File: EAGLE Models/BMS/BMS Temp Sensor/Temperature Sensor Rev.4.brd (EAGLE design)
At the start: 16 x 22 mm, 7 parts

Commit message: Set Resistance Values for the Temp Sense Board and Fixed ADC Connections
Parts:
- R2: value (none) -> 10k
- T$1: value THERMISTOR -> 10k
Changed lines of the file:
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@@
 <element name="G_OUT" library="wirepad" package="1,6/0,8" value="" x="2.54" y="3.81"/>
 <element name="OUTPUT" library="wirepad" package="1,6/0,8" value="" x="12.7" y="3.81"/>
-<element name="R2" library="resistor" package="R0603" value="" x="4.445" y="11.43" rot="R90"/>
-<element name="T$1" library="formula electric" package="0603" value="THERMISTOR" x="9.525" y="11.43" rot="R270"/>
+<element name="R2" library="resistor" package="R0603" value="10k" x="4.445" y="11.43" rot="R90"/>
+<element name="T$1" library="formula electric" package="0603" value="10k" x="9.525" y="11.43" rot="R270"/>
 <element name="VCC_IN" library="wirepad" package="1,6/0,8" value="" x="7.62" y="15.875"/>
 <element name="VCC_OUT" library="wirepad" package="1,6/0,8" value="" x="7.62" y="3.81"/>

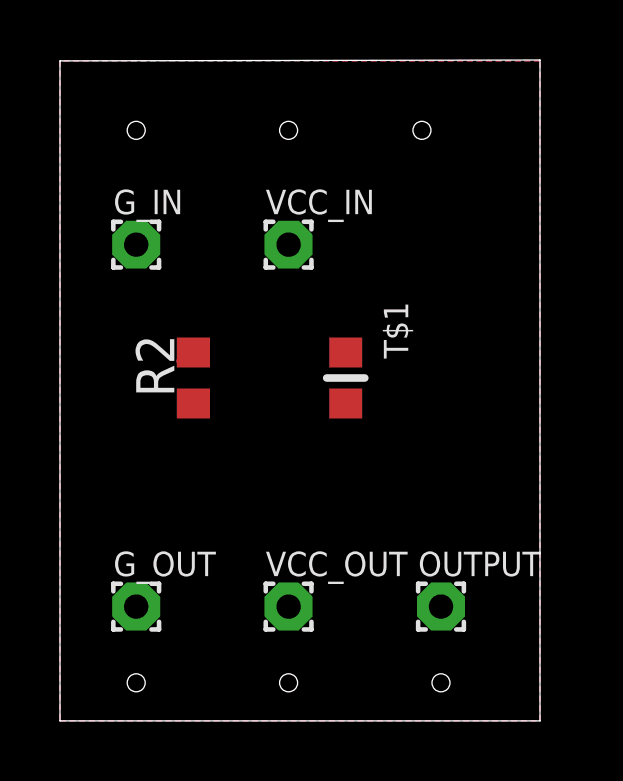
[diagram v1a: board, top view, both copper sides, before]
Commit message: Temp Sense Board Layouts Finished First revision, bunch of test layouts to get estimate of board sizes
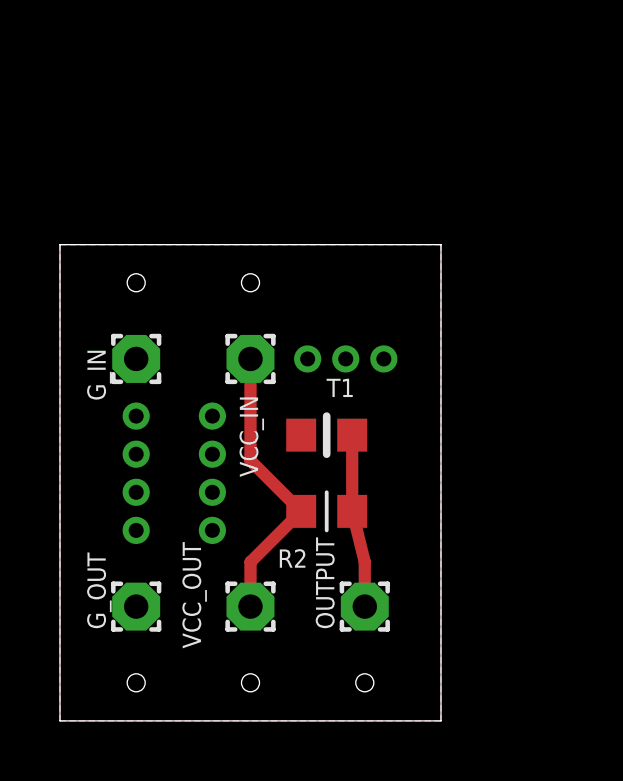
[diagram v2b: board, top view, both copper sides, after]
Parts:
- removed T$1: 10k, formula electric:0603
- added T1: 10k, formula electric:0603
- moved R2 6.29 mm to (8.89, 6.99), turned to 0 degrees
- moved VCC_IN 4.02 mm to (6.35, 12.1), turned to 90 degrees
- moved G_IN 3.81 mm to (2.54, 12.1), turned to 90 degrees
- moved OUTPUT 2.54 mm to (10.2, 3.81), turned to 90 degrees
- moved VCC_OUT 1.27 mm to (6.35, 3.81), turned to 90 degrees
- turned G_OUT to 90 degrees
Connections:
- net GND: now also T1.P$2; no longer T$1.P$2
- net OUTPUT: now also T1.P$1; no longer T$1.P$1
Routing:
- net VCC: track 0.00 -> 9.66 mm
- net OUTPUT: track 0.53 -> 5.77 mm
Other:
- board size 16 x 22 mm -> 12.7 x 15.9 mm
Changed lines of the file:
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@@
 <setting verticaltext="up"/>
 </settings>
-<grid distance="0.05" unitdist="inch" unit="mm" style="lines" multiple="1" display="no" altdistance="0.025" altunitdist="inch" altunit="inch"/>
+<grid distance="0.05" unitdist="inch" unit="inch" style="lines" multiple="1" display="no" altdistance="0.025" altunitdist="inch" altunit="inch"/>
 <layers>
 <layer number="1" name="Top" color="4" fill="1" visible="yes" active="yes"/>
@@
 <board>
 <plain>
-<wire x1="0" y1="0" x2="16" y2="0" width="0" layer="20"/>
-<wire x1="16" y1="0" x2="16" y2="22.03" width="0" layer="20"/>
-<wire x1="16" y1="22.03" x2="0" y2="22" width="0" layer="20"/>
-<wire x1="0" y1="22" x2="0" y2="0" width="0" layer="20"/>
+<wire x1="0" y1="0" x2="12.7" y2="0" width="0" layer="20"/>
+<wire x1="12.7" y1="0" x2="12.7" y2="15.875" width="0" layer="20"/>
+<wire x1="12.7" y1="15.875" x2="0" y2="15.875" width="0" layer="20"/>
+<wire x1="0" y1="15.875" x2="0" y2="0" width="0" layer="20"/>
 <hole x="2.54" y="1.27" drill="0.6"/>
-<hole x="7.62" y="1.27" drill="0.6"/>
-<hole x="12.7" y="1.27" drill="0.6"/>
-<hole x="12.065" y="19.685" drill="0.6"/>
-<hole x="7.62" y="19.685" drill="0.6"/>
-<hole x="2.54" y="19.685" drill="0.6"/>
+<hole x="6.35" y="1.27" drill="0.6"/>
+<hole x="10.16" y="1.27" drill="0.6"/>
+<hole x="6.35" y="14.605" drill="0.6"/>
+<hole x="2.54" y="14.605" drill="0.6"/>
 </plain>
 <attributes>
@@
 </class>
 </classes>
-<designrules name="default">
+<designrules name="default *">
 <description language="de">&lt;b&gt;EAGLE Design Rules&lt;/b&gt;
 &lt;p&gt;
@@
 <param name="mtCopper" value="0.035mm 0.035mm 0.035mm 0.035mm 0.035mm 0.035mm 0.035mm 0.035mm 0.035mm 0.035mm 0.035mm 0.035mm 0.035mm 0.035mm 0.035mm 0.035mm"/>
 <param name="mtIsolate" value="1.5mm 0.15mm 0.2mm 0.15mm 0.2mm 0.15mm 0.2mm 0.15mm 0.2mm 0.15mm 0.2mm 0.15mm 0.2mm 0.15mm 0.2mm"/>
-<param name="mdWireWire" value="8mil"/>
-<param name="mdWirePad" value="8mil"/>
-<param name="mdWireVia" value="8mil"/>
-<param name="mdPadPad" value="8mil"/>
-<param name="mdPadVia" value="8mil"/>
-<param name="mdViaVia" value="8mil"/>
-<param name="mdSmdPad" value="8mil"/>
-<param name="mdSmdVia" value="8mil"/>
-<param name="mdSmdSmd" value="8mil"/>
+<param name="mdWireWire" value="6mil"/>
+<param name="mdWirePad" value="6mil"/>
+<param name="mdWireVia" value="6mil"/>
+<param name="mdPadPad" value="6mil"/>
+<param name="mdPadVia" value="6mil"/>
+<param name="mdViaVia" value="6mil"/>
+<param name="mdSmdPad" value="6mil"/>
+<param name="mdSmdVia" value="6mil"/>
+<param name="mdSmdSmd" value="6mil"/>
 <param name="mdViaViaSameLayer" value="8mil"/>
 <param name="mnLayersViaInSmd" value="2"/>
@@
 <param name="mdDrill" value="8mil"/>
 <param name="mdSmdStop" value="0mil"/>
-<param name="msWidth" value="10mil"/>
-<param name="msDrill" value="24mil"/>
+<param name="msWidth" value="6mil"/>
+<param name="msDrill" value="13mil"/>
 <param name="msMicroVia" value="9.99mm"/>
 <param name="msBlindViaRatio" value="0.5"/>
@@
 <param name="srMinRoundness" value="0mil"/>
 <param name="srMaxRoundness" value="0mil"/>
-<param name="slThermalIsolate" value="10mil"/>
+<param name="slThermalIsolate" value="6mil"/>
 <param name="slThermalsForVias" value="0"/>
 <param name="dpMaxLengthDifference" value="10mm"/>
@@
 </autorouter>
 <elements>
-<element name="G_IN" library="wirepad" package="1,6/0,8" value="" x="2.54" y="15.875"/>
-<element name="G_OUT" library="wirepad" package="1,6/0,8" value="" x="2.54" y="3.81"/>
-<element name="OUTPUT" library="wirepad" package="1,6/0,8" value="" x="12.7" y="3.81"/>
-<element name="R2" library="resistor" package="R0603" value="10k" x="4.445" y="11.43" rot="R90"/>
-<element name="T$1" library="formula electric" package="0603" value="10k" x="9.525" y="11.43" rot="R270"/>
-<element name="VCC_IN" library="wirepad" package="1,6/0,8" value="" x="7.62" y="15.875"/>
-<element name="VCC_OUT" library="wirepad" package="1,6/0,8" value="" x="7.62" y="3.81"/>
+<element name="G_IN" library="wirepad" package="1,6/0,8" value="" x="2.54" y="12.065" smashed="yes" rot="R90">
+<attribute name="NAME" x="1.524" y="10.668" size="0.6096" layer="25" ratio="10" rot="R90"/>
+<attribute name="VALUE" x="1.94" y="12.065" size="0.0254" layer="27" rot="R90"/>
+</element>
+<element name="G_OUT" library="wirepad" package="1,6/0,8" value="" x="2.54" y="3.81" smashed="yes" rot="R90">
+<attribute name="NAME" x="1.524" y="3.048" size="0.6096" layer="25" ratio="10" rot="R90"/>
+<attribute name="VALUE" x="1.94" y="3.81" size="0.0254" layer="27" rot="R90"/>
+</element>
+<element name="OUTPUT" library="wirepad" package="1,6/0,8" value="" x="10.16" y="3.81" smashed="yes" rot="R90">
+<attribute name="NAME" x="9.144" y="3.048" size="0.6096" layer="25" ratio="10" rot="R90"/>
+<attribute name="VALUE" x="9.56" y="3.81" size="0.0254" layer="27" rot="R90"/>
+</element>
+<element name="R2" library="resistor" package="R0603" value="10k" x="8.89" y="6.985" smashed="yes">
+<attribute name="NAME" x="8.255" y="5.715" size="0.6096" layer="25" rot="R180"/>
+<attribute name="VALUE" x="10.795" y="7.62" size="0.6096" layer="27" rot="R270"/>
+</element>
+<element name="T1" library="formula electric" package="0603" value="10k" x="8.89" y="9.525" smashed="yes" rot="R180">
+<attribute name="NAME" x="8.89" y="10.795" size="0.6096" layer="25"/>
+<attribute name="VALUE" x="10.795" y="10.16" size="0.6096" layer="27" rot="R270"/>
+</element>
+<element name="VCC_IN" library="wirepad" package="1,6/0,8" value="" x="6.35" y="12.065" smashed="yes" rot="R90">
+<attribute name="NAME" x="6.604" y="8.128" size="0.6096" layer="25" ratio="10" rot="R90"/>
+<attribute name="VALUE" x="5.75" y="12.065" size="0.0254" layer="27" rot="R90"/>
+</element>
+<element name="VCC_OUT" library="wirepad" package="1,6/0,8" value="" x="6.35" y="3.81" smashed="yes" rot="R90">
+<attribute name="NAME" x="4.699" y="2.413" size="0.6096" layer="25" ratio="10" rot="R90"/>
+<attribute name="VALUE" x="5.75" y="3.81" size="0.0254" layer="27" rot="R90"/>
+</element>
 </elements>
 <signals>
@@
 <contactref element="VCC_IN" pad="1"/>
 <contactref element="VCC_OUT" pad="1"/>
-<wire x1="4.445" y1="10.58" x2="7.62" y2="15.875" width="0" layer="19" extent="16-16"/>
-<wire x1="7.62" y1="3.81" x2="4.445" y2="10.58" width="0" layer="19" extent="16-16"/>
+<wire x1="6.35" y1="3.81" x2="6.35" y2="5.295" width="0.4064" layer="1"/>
+<wire x1="6.35" y1="5.295" x2="8.04" y2="6.985" width="0.4064" layer="1"/>
+<wire x1="8.04" y1="6.985" x2="6.35" y2="8.675" width="0.4064" layer="1"/>
+<wire x1="6.35" y1="8.675" x2="6.35" y2="12.065" width="0.4064" layer="1"/>
 </signal>
 <signal name="GND">
-<contactref element="T$1" pad="P$2"/>
+<contactref element="T1" pad="P$2"/>
 <contactref element="G_IN" pad="1"/>
 <contactref element="G_OUT" pad="1"/>
 <polygon width="0.4064" layer="1" isolate="0.3048">
 <vertex x="0" y="0"/>
-<vertex x="16" y="0"/>
-<vertex x="16" y="22"/>
-<vertex x="0" y="22"/>
+<vertex x="12.7" y="0"/>
+<vertex x="12.7" y="15.875"/>
+<vertex x="0" y="15.875"/>
 </polygon>
 <polygon width="0.4064" layer="16" isolate="0.3048">
 <vertex x="0" y="0"/>
-<vertex x="16" y="0"/>
-<vertex x="16" y="22"/>
-<vertex x="0" y="22"/>
+<vertex x="12.7" y="0"/>
+<vertex x="12.7" y="15.875"/>
+<vertex x="0" y="15.875"/>
 </polygon>
-<wire x1="9.525" y1="10.58" x2="2.54" y2="15.875" width="0" layer="19" extent="1-1"/>
-<wire x1="2.54" y1="3.81" x2="9.525" y2="10.58" width="0" layer="19" extent="1-1"/>
+<via x="2.54" y="10.16" extent="1-16" drill="0.5"/>
+<via x="2.54" y="8.89" extent="1-16" drill="0.5"/>
+<via x="2.54" y="7.62" extent="1-16" drill="0.5"/>
+<via x="2.54" y="6.35" extent="1-16" drill="0.5"/>
+<via x="5.08" y="6.35" extent="1-16" drill="0.5"/>
+<via x="5.08" y="7.62" extent="1-16" drill="0.5"/>
+<via x="5.08" y="8.89" extent="1-16" drill="0.5"/>
+<via x="5.08" y="10.16" extent="1-16" drill="0.5"/>
+<via x="8.255" y="12.065" extent="1-16" drill="0.5"/>
+<via x="9.525" y="12.065" extent="1-16" drill="0.5"/>
+<via x="10.795" y="12.065" extent="1-16" drill="0.5"/>
 </signal>
 <signal name="OUTPUT">
 <contactref element="OUTPUT" pad="1"/>
-<contactref element="T$1" pad="P$1"/>
+<contactref element="T1" pad="P$1"/>
 <contactref element="R2" pad="2"/>
-<wire x1="4" y1="12" x2="4.445" y2="12.28" width="0.254" layer="1"/>
-<wire x1="9.525" y1="12.28" x2="12.7" y2="3.81" width="0" layer="19" extent="1-1"/>
-<wire x1="9.525" y1="12.28" x2="4.445" y2="12.28" width="0" layer="19" extent="1-16"/>
+<wire x1="10.16" y1="3.81" x2="10.16" y2="5.295" width="0.4064" layer="1"/>
+<wire x1="10.16" y1="5.295" x2="9.74" y2="6.985" width="0.4064" layer="1"/>
+<wire x1="9.74" y1="6.985" x2="9.74" y2="9.525" width="0.4064" layer="1"/>
 </signal>
 </signals>
+<errors>
+</errors>
 </board>
 </drawing>
